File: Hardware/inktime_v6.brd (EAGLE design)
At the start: 46 x 35 mm, 89 parts, among them IC1 BQ25180YBGR, IC2 DRV2605YZFR, IC3 BMA421, IC9 RT6160AWSC, J1 503480-2400, J2 TC2030-IDC, J4 KH-TYPE-C-16P, Q3 DMG2305UX-7, U1 nRF52840-QIAA-R, U3 MAX17048G+T10, X1 32MHz, X2 32.768kHz

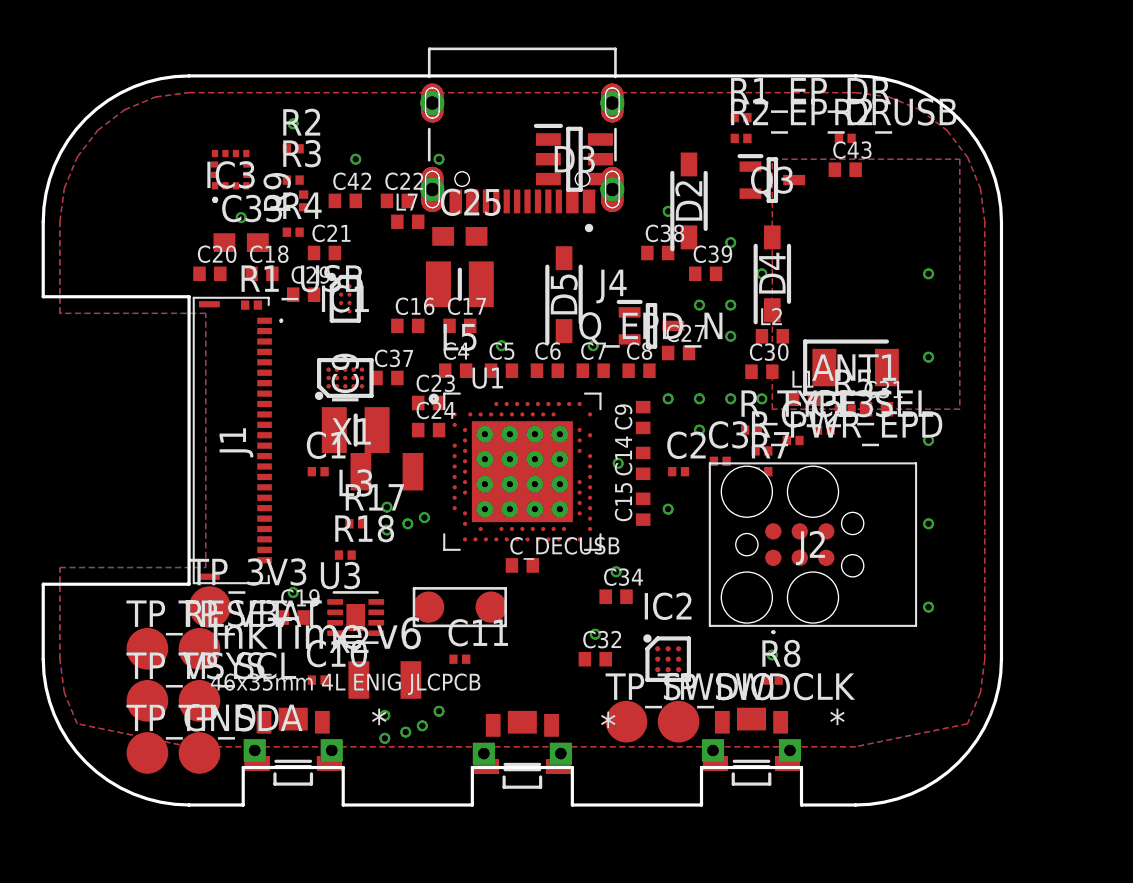
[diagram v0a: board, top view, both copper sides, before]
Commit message: Update BOM and CPL from final PCB
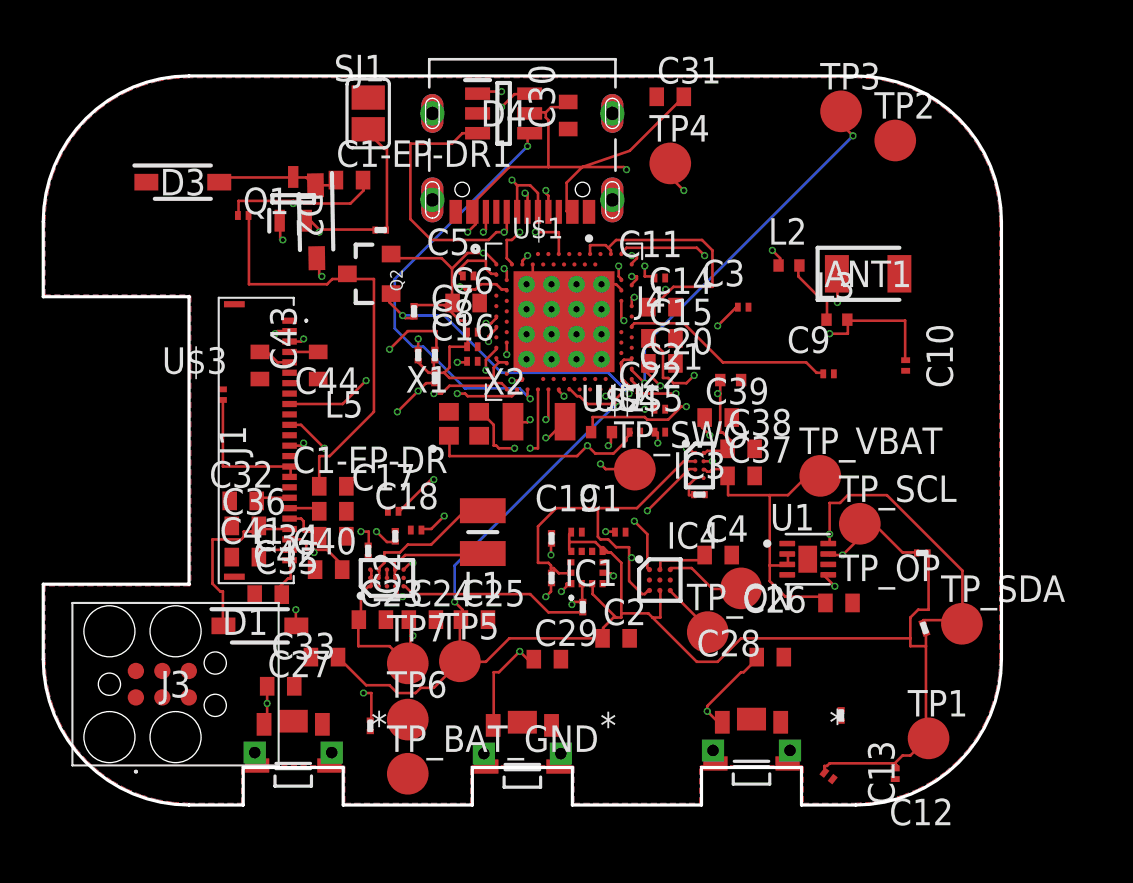
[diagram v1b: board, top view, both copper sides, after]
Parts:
- removed C_DECUSB: 4.7uF, inktime_v5:PERFECT_0402_0402
- removed D5: MBR0530, inktime_v5:ESP32_C6_LIBRARY_5_SOD3716X135N
- removed IC9: RT6160AWSC, inktime_v5:RT6160AWSC_BGA15C40P3X5_140X230X60
- removed J2: TC2030-IDC, inktime_v5:TC2030-IDC_TC2030IDC
- removed L7: 470mOhm, inktime_v5:PERFECT_0402_0402
- removed MOT1: LCM1027B3605F, inktime_v5:WIRE
- removed Q3: DMG2305UX-7, inktime_v5:ESP32_C6_LIBRARY_6_SOT65P210X110-3N
- removed Q_EPD_N: SI1308EDL-T1-GE3, inktime_v5:ESP32_C6_LIBRARY_6_SOT65P210X110-3N
- removed R17, R18: 3.3k, inktime_v5:NORDIC_NRF_2_RESC0201_N
- removed R1_EP_DR, R2_EP_DR, R_PWR_EPD: 10k, inktime_v5:NORDIC_NRF_2_RESC0201_N
- removed R1_USB, R2_USB: 5.1k, inktime_v5:NORDIC_NRF_2_RESC0201_N
- removed R_TYPE_SEL: 2.2, inktime_v5:NORDIC_NRF_2_RESC0201_N
- removed SW_DN, SW_ENT, SW_UP: SW_PUSH, inktime_v5:2025-10-22_07-23-44_LIBRARY_SW_EVP-AKE31A_PAN
- removed TP_3V3, TP_GND, TP_RESET, TP_SWDCLK, TP_SWDIO, TP_VSYS: TP, inktime_v5:HECTOR_WATCH_1_TP20R
- removed U3: MAX17048G+T10, inktime_v5:ESP32_C6_LIBRARY_SON50P200X200X80-9N
- added C1-EP-DR: 10uF, dan-tudose-lib:ESP32_C6_LIBRARY_1_ESP32_WROVER_EAGLE-LTSPICE_C0402
- added C1-EP-DR1: 4.7uF/25V, dan-tudose-lib:ESP32_C6_LIBRARY_1_ESP32_WROVER_EAGLE-LTSPICE_C0402
- added C26: 0.1uF, dan-tudose-lib:ESP32_C6_LIBRARY_1_ESP32_WROVER_EAGLE-LTSPICE_C0402
- added C28: 1uF, dan-tudose-lib:ESP32_C6_LIBRARY_1_ESP32_WROVER_EAGLE-LTSPICE_C0402
- added C35, C36, C40, C41, C44: 1uF/50V, dan-tudose-lib:ESP32_C6_LIBRARY_1_ESP32_WROVER_EAGLE-LTSPICE_C0402
- added D1: ESP32_C6_LIBRARY_5_MBR0530, dan-tudose-lib:ESP32_C6_LIBRARY_5_SOD3716X135N
- added IC4: DRV2605YZFR_DRV2605YZFR, dan-tudose-lib:DRV2605YZFR_BGA9C50P3X3_144X144X62
- added J3: TC2030-IDC_TC2030-IDC, dan-tudose-lib:TC2030-IDC_TC2030IDC
- added Q1: ESP32_C6_LIBRARY_6_SI1308EDL-T1-GE3, dan-tudose-lib:ESP32_C6_LIBRARY_6_SOT65P210X110-3N
- added Q2: 20V/4.2A/52mΩ/1.4W, dan-tudose-lib:ESP32_C6_LIBRARY_4_ESP32_C6_LIBRARY_4_ESP32_C6_LIBRARY_4_ESP32_C6_LIBRARY_4_ESP32_WROVER_SPARKFUN-DISCRE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
- added R1: 0, dan-tudose-lib:CPF0201D7K68C1_0201
- added R10, R11, R12, R13, R14, R16: 10K, dan-tudose-lib:CPF0201D7K68C1_0201
- added R6: 0.47, dan-tudose-lib:CPF0201D7K68C1_0201
- added SJ1: 0, dan-tudose-lib:ESP32_C6_LIBRARY_7_JUMPER_SJ
- added SW1, SW2, SW3: 2025-10-22_07-23-44_LIBRARY_EVP-AKE31ASW_EVP-AKE31A_PAN, dan-tudose-lib:2025-10-22_07-23-44_LIBRARY_SW_EVP-AKE31A_PAN
- added TP1, TP2, TP3, TP4, TP5, TP6, TP7, TP_BAT_GND, TP_ON, TP_OP, TP_SWO: HECTOR_WATCH_1_TPTP20R, dan-tudose-lib:HECTOR_WATCH_1_TP20R
- added U$1: NORDIC_NRF_4_NRF52840_QF, dan-tudose-lib:NORDIC_NRF_4_AQFN50P700X700X85_HS-74N
- added U$2: 3.9nH, dan-tudose-lib:NORDIC_NRF_2_RESC0402_L
- added U$3: 1uF/50V, dan-tudose-lib:NORDIC_NRF_3_RESC0201_L
- added U$4, U$5: 12pF, dan-tudose-lib:NORDIC_NRF_3_RESC0201_L
- ANT1: value 2450AT18B100E -> 2450AT18B100E_2450AT18B100E; device inktime_v5:2450AT18B100E_ANTC3216X140N -> dan-tudose-lib:2450AT18B100E_ANTC3216X140N
- C1: value 12pF -> 1pF; device inktime_v5:NORDIC_NRF_2_RESC0201_N -> dan-tudose-lib:NORDIC_NRF_3_RESC0201_L
- C10: value 12pF -> N.C.; device inktime_v5:NORDIC_NRF_2_RESC0201_N -> dan-tudose-lib:NORDIC_NRF_3_RESC0201_L
- C11: value 12pF -> 100pF; device inktime_v5:NORDIC_NRF_2_RESC0201_N -> dan-tudose-lib:NORDIC_NRF_3_RESC0201_L
- C12: value 820pF -> 100nF; device inktime_v5:NORDIC_NRF_2_RESC0201_N -> dan-tudose-lib:NORDIC_NRF_3_RESC0201_L
- C13: value 1pF -> N.C.; device inktime_v5:NORDIC_NRF_2_RESC0201_N -> dan-tudose-lib:NORDIC_NRF_3_RESC0201_L
- C14, C6: value 100nF -> 4.7µF; device inktime_v5:PERFECT_0402_0402 -> dan-tudose-lib:ESP32_C6_LIBRARY_1_ESP32_WROVER_EAGLE-LTSPICE_C0402
- C15: value 100nF -> 1.0µF; device inktime_v5:PERFECT_0402_0402 -> dan-tudose-lib:ESP32_C6_LIBRARY_1_ESP32_WROVER_EAGLE-LTSPICE_C0402
- C16: value 4.7uF -> 47nF; device inktime_v5:PERFECT_0402_0402 -> dan-tudose-lib:NORDIC_NRF_3_RESC0201_L
- C17: value 4.7uF -> 12pF; device inktime_v5:PERFECT_0402_0402 -> dan-tudose-lib:NORDIC_NRF_3_RESC0201_L
- C18: value 47nF -> 12pF; device inktime_v5:PERFECT_0402_0402 -> dan-tudose-lib:NORDIC_NRF_3_RESC0201_L
- C19, C5: device inktime_v5:PERFECT_0402_0402 -> dan-tudose-lib:NORDIC_NRF_3_RESC0201_L
- C2: value 12pF -> 0.1uF; device inktime_v5:NORDIC_NRF_2_RESC0201_N -> dan-tudose-lib:ESP32_C6_LIBRARY_1_ESP32_WROVER_EAGLE-LTSPICE_C0402
- C20: value 4.7uF -> 4.7µF; device inktime_v5:PERFECT_0402_0402 -> dan-tudose-lib:ESP32_C6_LIBRARY_1_ESP32_WROVER_EAGLE-LTSPICE_C0402
- C21: value 1uF -> 4.7µF; device inktime_v5:PERFECT_0402_0402 -> dan-tudose-lib:NORDIC_NRF_3_RESC0402_L
- C22: value 0.1uF -> N.C.; device inktime_v5:PERFECT_0402_0402 -> dan-tudose-lib:NORDIC_NRF_3_RESC0201_L
- C23, C24, C38: device inktime_v5:PERFECT_0402_0402 -> dan-tudose-lib:ESP32_C6_LIBRARY_1_ESP32_WROVER_EAGLE-LTSPICE_C0402
- C25, C33: device inktime_v5:NORDIC_NRF_2_RESC0603_N -> dan-tudose-lib:ESP32_C6_LIBRARY_1_ESP32_WROVER_EAGLE-LTSPICE_C0402
- C27, C29: value 1uF/50V -> 1uF; device inktime_v5:PERFECT_0402_0402 -> dan-tudose-lib:ESP32_C6_LIBRARY_1_ESP32_WROVER_EAGLE-LTSPICE_C0402
- C3: device inktime_v5:NORDIC_NRF_2_RESC0201_N -> dan-tudose-lib:NORDIC_NRF_3_RESC0201_L
- C30: value 0.1uF/50V -> 4.7uF; device inktime_v5:PERFECT_0402_0402 -> dan-tudose-lib:ESP32_C6_LIBRARY_1_ESP32_WROVER_EAGLE-LTSPICE_C0402
- C31: value 1uF/50V -> 0.1uF; device inktime_v5:PERFECT_0402_0402 -> dan-tudose-lib:ESP32_C6_LIBRARY_1_ESP32_WROVER_EAGLE-LTSPICE_C0402
- C32: value 1uF -> 1uF/50V; device inktime_v5:PERFECT_0402_0402 -> dan-tudose-lib:ESP32_C6_LIBRARY_1_ESP32_WROVER_EAGLE-LTSPICE_C0402
- C34, C43: value 0.1uF -> 1uF/50V; device inktime_v5:PERFECT_0402_0402 -> dan-tudose-lib:ESP32_C6_LIBRARY_1_ESP32_WROVER_EAGLE-LTSPICE_C0402
- C37: value 10uF -> 1uF; device inktime_v5:PERFECT_0402_0402 -> dan-tudose-lib:ESP32_C6_LIBRARY_1_ESP32_WROVER_EAGLE-LTSPICE_C0402
- C39: value 100nF -> 10uF; device inktime_v5:PERFECT_0402_0402 -> dan-tudose-lib:ESP32_C6_LIBRARY_1_ESP32_WROVER_EAGLE-LTSPICE_C0402
- C4: value 100nF -> 1uF; device inktime_v5:PERFECT_0402_0402 -> dan-tudose-lib:ESP32_C6_LIBRARY_1_ESP32_WROVER_EAGLE-LTSPICE_C0402
- C42: value 4.7uF -> 1uF/50V; device inktime_v5:PERFECT_0402_0402 -> dan-tudose-lib:ESP32_C6_LIBRARY_1_ESP32_WROVER_EAGLE-LTSPICE_C0402
- C7: value 100pF -> 100nF; device inktime_v5:PERFECT_0402_0402 -> dan-tudose-lib:NORDIC_NRF_3_RESC0201_L
- C8: value 4.7uF -> 100nF; device inktime_v5:PERFECT_0402_0402 -> dan-tudose-lib:NORDIC_NRF_3_RESC0201_L
- C9: value 1uF -> 820pF; device inktime_v5:PERFECT_0402_0402 -> dan-tudose-lib:NORDIC_NRF_3_RESC0201_L
- D2: value MBR0530 -> ESP32_C6_LIBRARY_5_MBR0530; device inktime_v5:ESP32_C6_LIBRARY_5_SOD3716X135N -> dan-tudose-lib:ESP32_C6_LIBRARY_5_SOD3716X135N
- D3: value USBLC6-2SC6Y -> ESP32_C6_LIBRARY_5_MBR0530; device inktime_v5:ESP32_C6_LIBRARY_3_SOT95P280X145-6N -> dan-tudose-lib:ESP32_C6_LIBRARY_5_SOD3716X135N
- D4: value MBR0530 -> ESP32_C6_LIBRARY_3_USBLC6-2SC6Y; device inktime_v5:ESP32_C6_LIBRARY_5_SOD3716X135N -> dan-tudose-lib:ESP32_C6_LIBRARY_3_SOT95P280X145-6N
- IC1: value BQ25180YBGR -> BMA423_BMA423; device inktime_v5:BQ25180YBGR_BGA8C40P2X4_100X155X50 -> dan-tudose-lib:BMA423_BMA423
- IC2: value DRV2605YZFR -> RT6160AWSC_RT6160AWSC; device inktime_v5:DRV2605YZFR_BGA9C50P3X3_144X144X62 -> dan-tudose-lib:RT6160AWSC_BGA15C40P3X5_140X230X60
- IC3: value BMA421 -> BQ25180YBGR_BQ25180YBGR; device inktime_v5:BMA423_BMA423 -> dan-tudose-lib:BQ25180YBGR_BGA8C40P2X4_100X155X50
- J1: value 503480-2400 -> 503480-2400_503480-2400; device inktime_v5:503480-2400_5034802400 -> dan-tudose-lib:503480-2400_5034802400
- J4: value KH-TYPE-C-16P -> KH-TYPE-C-16P_KH-TYPE-C-16P; device inktime_v5:KH-TYPE-C-16P_KINGHELM_KH-TYPE-C-16P -> dan-tudose-lib:KH-TYPE-C-16P_KINGHELM_KH-TYPE-C-16P
- L1: value 3.9nH -> MLP2016SR47MT0S1_FTC252012SR47MBCA; device inktime_v5:PERFECT_0402_0402 -> dan-tudose-lib:MLP2016SR47MT0S1_INDC2016X100N
- L2: value 15nH -> 10µH; device inktime_v5:PERFECT_0402_0402 -> dan-tudose-lib:NORDIC_NRF_2_RESC0402_L
- L3: value 10uH -> 10µH; device inktime_v5:MLP2016SR47MT0S1_INDC2016X100N -> dan-tudose-lib:NORDIC_NRF_2_RESC0402_L
- L5: device inktime_v5:MLP2016SR47MT0S1_INDC2016X100N -> dan-tudose-lib:NORDIC_NRF_2_RESC0201_L
- R2, R3: device inktime_v5:NORDIC_NRF_2_RESC0201_N -> dan-tudose-lib:CPF0201D7K68C1_0201
- R4: value 0 -> 3K3; device inktime_v5:NORDIC_NRF_2_RESC0201_N -> dan-tudose-lib:CPF0201D7K68C1_0201
- R5: value 10k -> 3K3; device inktime_v5:NORDIC_NRF_2_RESC0201_N -> dan-tudose-lib:CPF0201D7K68C1_0201
- R7: value 10k -> 2.2; device inktime_v5:NORDIC_NRF_2_RESC0201_N -> dan-tudose-lib:CPF0201D7K68C1_0201
- R8, R9: value 10k -> 10K; device inktime_v5:NORDIC_NRF_2_RESC0201_N -> dan-tudose-lib:CPF0201D7K68C1_0201
- TP_SCL, TP_SDA, TP_VBAT: value TP -> HECTOR_WATCH_1_TPTP20R; device inktime_v5:HECTOR_WATCH_1_TP20R -> dan-tudose-lib:HECTOR_WATCH_1_TP20R
- U1: value nRF52840-QIAA-R -> ESP32_C6_LIBRARY_MAX17048G+T10; device inktime_v5:NORDIC_NRF_4_AQFN50P700X700X85_HS-74N -> dan-tudose-lib:ESP32_C6_LIBRARY_SON50P200X200X80-9N
- X1: device inktime_v5:NORDIC_NRF_1_XTAL_3215_N -> dan-tudose-lib:NORDIC_NRF_BT-XTAL_2016_N
- X2: device inktime_v5:NORDIC_NRF_1_XTAL_3215_N -> dan-tudose-lib:NORDIC_NRF_1_XTAL_3215_N
- moved TP_SDA 37.1 mm to (21.1, -8.80)
- moved R4 33.9 mm to (19.2, -5.40), turned to 270 degrees
- moved TP_SCL 32.8 mm to (16.2, -4.00)
- moved C10 32.0 mm to (18.4, 3.60), turned to 270 degrees
- moved TP_VBAT 30.9 mm to (14.3, -1.70)
- moved C43 27.0 mm to (-9.80, 3.60), turned to 90 degrees
- moved IC3 26.6 mm to (8.50, -1.20)
- moved C27 24.9 mm to (-11.6, -11.8)
- moved R2 24.0 mm to (1.40, -6.60)
- moved L3 23.7 mm to (15.1, 5.80)
- moved R9 23.7 mm to (8.50, -2.60), turned to 270 degrees
- moved C20 22.1 mm to (6.70, 3.70)
- moved R3 21.2 mm to (1.40, -4.70)
- moved C29 21.1 mm to (1.20, -10.5)
- moved C11 20.7 mm to (6.60, 7.80)
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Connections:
- removed net BTN_DN: R7.2, SW_DN.1, U1.P$AC9
- removed net BTN_ENT: R8.2, SW_ENT.1, U1.P$AD22
- removed net BTN_UP: R5.2, SW_UP.1, U1.P$AD8
- removed net DCC_LX: U1.P$B3
- removed net DEC1: C4.1, U1.P$C1
- removed net DECUSB: C_DECUSB.1, U1.P$N24
- removed net EPD_C1: C29.1, J1.2
- removed net EPD_C2: C31.1, J1.1
- removed net EPD_MOSI: J1.21, U1.P$B13
- removed net EPD_PWR_EN: Q3.1, R_PWR_EPD.2, U1.P$Y23
- removed net EPD_SCK: J1.20, U1.P$A12
- removed net FUEL_ALRT: U1.P$J24, U3.5
- removed net HAPTIC_OUT_N: IC2.C3, MOT1.-
- removed net HAPTIC_OUT_P: IC2.A3, MOT1.+
- removed net LX_EPD: D2.1, D4.1, L5.1, Q_EPD_N.3
- removed net RF_ANT: ANT1.1, C12.1, C13.1, C3.1, L1.2, L2.1, U1.P$H23
- removed net RF_LX1: IC9.B2, IC9.B3, L1.1, L3.1
- removed net RF_LX2: IC9.D2, IC9.D3, L2.2, L3.2
- removed net USB_CC1: J4.A5, R1_USB.1
- removed net USB_CC2: J4.B5, R2_USB.1
- removed net USB_DM: D3.2, D3.4, J4.A7, J4.B7, U1.P$AD4
- removed net USB_DP: D3.1, D3.6, J4.A6, J4.B6, U1.P$AD6
- removed net VSYS: C17.1, C20.1, C22.1, C23.1, IC1.B2, IC9.A1, IC9.A2, IC9.A3, L7.1, L7.2, TP_VSYS.TP
- removed net XC1_32K: C1.1, U1.P$B24, X1.1
- removed net XC2_32K: C2.1, U1.P$A23, X1.2
- removed net XL1: C10.1, U1.P$D2, X2.1
- removed net XL2: C11.1, U1.P$F2, X2.2
- removed net nRESET: J2.3, TP_RESET.TP, U1.P$AC13
- new net ALERT: U$1.P$J24, U1.5
- new net D+: D4.4, U$1.P$AD6
- new net D-: D4.6, U$1.P$AD4
- new net DEC3: C11.1, U$1.P$D23
- new net DN: D4.1, J4.A7, J4.B7
- new net DP: D4.3, J4.A6, J4.B6
- new net EPD: J1.15, J1.16, U$3.2
- new net GDR: J1.2, Q1.1, R8.2
- new net GND3: IC1.1, R3.2
- new net LX1: IC2.B2, IC2.B3, L1.1
- new net LX2: IC2.D2, IC2.D3, L1.2
- new net MOSI: J1.14, U$1.P$B13
- new net N$1: C5.1, U$1.P$C1
- new net N$10: IC2.D1, R2.2
- new net N$11: C1-EP-DR1.2, D1.2, L5.2
- new net N$12: IC2.E1, R1.2
- new net N$13: C1-EP-DR1.1, D2.1, D3.2, Q1.3
- new net N$14: C9.1, U$1.P$N24
- new net N$16: IC3.D1, R9.2
- new net N$21: U$1.P$B24, U$4.1, X1.1
- new net N$22: R6.1, SJ1.2
- new net N$24: L2.1, U$1.P$B3
- new net N$3: C20.1, U$1.P$AC5
- new net N$30: C4.1, IC4.A2
- new net N$4: ANT1.1, C1.1, C22.1, U$2.2
- new net N$45: J4.A5, R13.2
- new net N$5: C3.1, U$1.P$H23, U$2.1
- new net N$52: J4.B5, R14.1
- new net N$59: C43.2, J1.4
- new net N$6: L2.2, L3.1
- new net N$60: C44.2, J1.5
- new net N$7: U$1.P$A23, U$5.1, X1.3
- new net N$70: C32.2, J1.18
- new net N$71: C34.2, J1.19
- new net N$72: C35.2, J1.20
- new net N$76: C41.2, J1.23
- new net N$78: C42.2, J1.24
- new net OUT+: IC4.A3, TP_OP.TP
- new net OUT-: IC4.C3, TP_ON.TP
- new net P0.00/XL1: C17.2, U$1.P$D2, X2.1
- new net P0.00/XL2: C18.2, U$1.P$F2, X2.2
- new net P0.04: U$1.P$J1
- new net P0.09: U$1.P$L24
- new net P0.13: C27.1, R10.1, SW1.2, U$1.P$AD8
- new net P0.14: C28.1, R11.1, SW2.2, U$1.P$AC9
- new net P0.19: U$1.P$AC15
- new net P0.20: U$1.P$AD16
- new net P0.21: U$1.P$AC17
- new net P0.22: U$1.P$AD18
- new net P0.23: U$1.P$AC19
- new net P0.24: U$1.P$AD20
- new net P0.25: U$1.P$AC21
- new net P0.26: U$1.P$G1
- new net P0.27: U$1.P$H2
- new net P0.28: U$1.P$B11
- new net P0.29: U$1.P$A10
- new net P0.30: U$1.P$B9
- new net P0.31: U$1.P$A8
- new net P1.01: Q2.1, R16.1, U$1.P$W24, U$1.P$Y23
- new net P1.02: C29.1, R12.1, SW3.2
- new net P1.03: U$1.P$V23
- new net P1.04: U$1.P$U24
- new net P1.05: U$1.P$T23
- new net P1.06: U$1.P$R24
- new net P1.07: U$1.P$P23
- new net P1.09: U$1.P$R1
- new net P1.10: U$1.P$A20
- new net P1.11: U$1.P$B19
- new net P1.12: U$1.P$B17
- new net P1.13: U$1.P$A16
- new net P1.14: U$1.P$B15
- new net P1.15: U$1.P$A14
- new net RESET: TP2.TP, U$1.P$AC13
- new net SCK: J1.13, U$1.P$A12
- new net SWO: TP_SWO.TP, U$1.P$AD22
- new net VREG: C23.1, C24.1, C39.1, IC2.A1, IC2.A2, IC2.A3, IC3.B2, TP7.TP
- net 3V3: now also C12.1, C13.1, C2.1, IC1.10, IC1.3, IC1.7, IC2.E3, IC4.C2, Q2.2, R10.2, R11.2, R12.2, R16.2, R4.1, TP1.TP, TP5.TP, U$1.P$A18, U$1.P$A22, U$1.P$AD14, U$1.P$AD23, U$1.P$B1, U$1.P$W1, U$1.P$Y2; no longer C15.1, C24.1, C32.1, C34.1, C5.1, IC2.C2, IC3.3, IC3.7, IC9.E2, IC9.E3, J2.1, Q3.2, R17.1, R18.1, R2.1, R2.2, R7.1, R8.1, R_PWR_EPD.1, TP_3V3.TP, U1.P$A22, U1.P$AD14, U1.P$AD23, U1.P$B1, U1.P$W1, U1.P$Y2
- net DEC4_6: now also C10.1, C15.1, C16.1, L3.2, U$1.P$B5, U$1.P$E24; no longer C9.1, U1.P$B5, U1.P$E24
- net EPD_3V3: now also C1-EP-DR.1, L5.1, Q2.3; no longer C27.1, C30.1, D4.2, D5.1, J1.24, L5.2, Q3.3, R1_EP_DR.1, R2_EP_DR.1, R_TYPE_SEL.1
- net EPD_BUSY: now also J1.9, U$1.P$AD12; no longer U1.P$AD12
- net EPD_CS: now also J1.12, U$1.P$K2; no longer J1.22, U1.P$K2
- net EPD_DC: now also J1.11, U$1.P$AD10; no longer J1.23, U1.P$AD10
- net EPD_RST: now also J1.10, U$1.P$AC11; no longer U1.P$AC11
- net GND: now also C1-EP-DR.2, C17.1, C18.1, C26.2, C28.2, C30.1, C31.1, C32.1, C34.1, C35.1, C36.1, C40.1, C41.1, C43.1, C44.1, D3.1, D4.2, IC1.8, IC1.9, IC2.B1, IC2.C1, IC2.C2, IC2.C3, IC3.D2, IC4.B1, IC4.B3, J1.17, J1.8, R13.1, R14.2, R7.1, R8.1, SJ1.1, SW1.1, SW2.1, SW3.1, TP6.TP, TP_BAT_GND.TP, U$1.P$74, U$1.P$75, U$1.P$76, U$1.P$77, U$1.P$78, U$1.P$79, U$1.P$80, U$1.P$81, U$1.P$82, U$1.P$83, U$1.P$84, U$1.P$85, U$1.P$86, U$1.P$87, U$1.P$88, U$1.P$89, U$1.P$90, U$1.P$B7, U$1.P$F23, U$3.1, U$4.2, U$5.2, U1.1, U1.4, U1.6, U1.9, X1.2, X1.4; no longer ANT1.2, C17.2, C18.2, C30.2, C31.2, C32.2, C34.2, C42.2, C43.2, C_DECUSB.2, D3.3, IC1.D1, IC1.D2, IC2.B3, IC3.1, IC3.8, IC3.9, IC9.B1, IC9.C1, IC9.C2, IC9.C3, J2.5, Q_EPD_N.2, R1_EP_DR.2, R1_USB.2, R2_EP_DR.2, R2_USB.2, R3.2, R9.2, R_TYPE_SEL.2, SW_DN.5, SW_ENT.5, SW_UP.5, TP_GND.TP, U1.P$74, U1.P$75, U1.P$76, U1.P$77, U1.P$78, U1.P$79, U1.P$80, U1.P$81, U1.P$82, U1.P$83, U1.P$84, U1.P$85, U1.P$86, U1.P$87, U1.P$88, U1.P$89, U1.P$90, U1.P$B7, U1.P$F23, U3.1, U3.4, U3.9
- net HAPTIC_EN: now also IC4.A1, U$1.P$U1; no longer IC2.A1, IC2.B1, U1.P$U1
- net IMU_INT1: now also IC1.5, U$1.P$N1; no longer IC3.5, U1.P$N1
- net IMU_INT2: now also IC1.6, U$1.P$P2; no longer IC3.6, U1.P$P2
- net PMIC_INT: now also IC3.A1, U$1.P$T2; no longer IC1.A1, U1.P$T2
- net PREVGH: now also C36.2, D1.1, J1.21; no longer D2.2
- net PREVGL: now also C40.2, D2.2, J1.22; no longer D5.2
- net RESE: now also J1.3, Q1.2, R6.2; no longer Q_EPD_N.1
- net SCL: now also IC1.12, IC3.B1, IC4.C1, R2.1, U$1.P$M2, U1.7; no longer IC1.B1, IC2.C1, IC3.11, IC3.12, IC9.D1, R18.2, R4.1, U1.P$M2, U3.7
- net SDA: now also IC1.2, IC3.C1, IC4.B2, R1.1, R5.2, U$1.P$L1, U1.8; no longer IC1.C1, IC2.B2, IC3.2, IC3.4, IC9.E1, R17.2, U1.P$L1, U3.8
- net SWDCLK: now also TP3.TP, U$1.P$AA24; no longer J2.4, TP_SWDCLK.TP, U1.P$AA24
- net SWDIO: now also TP4.TP, U$1.P$AC24; no longer J2.2, TP_SWDIO.TP, U1.P$AC24
- net VBAT: now also C26.1, IC3.C2, U1.2, U1.3; no longer C18.1, C38.1, IC1.C2, U3.2, U3.3
- net VBUS: now also C30.2, C31.2, C38.1, D4.5, IC3.A2, U$1.P$AD2; no longer C16.1, C42.1, C43.1, D3.5, IC1.A2, U1.P$AD2
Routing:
- net 3V3: track 0.00 -> 132.0 mm, vias 11 -> 5
- net VBUS: track 0.00 -> 56.4 mm, vias 0 -> 4
- net SDA: track 0.00 -> 49.8 mm, vias 0 -> 4
- net DEC4_6: track 0.00 -> 39.5 mm, vias 0 -> 5
- net P0.13: track 0.00 -> 37.6 mm, vias 0 -> 4
- net P0.14: track 0.00 -> 36.3 mm, vias 0 -> 2
- net SCL: track 0.00 -> 35.2 mm, vias 0 -> 2
- net VREG: track 0.00 -> 31.3 mm, vias 0 -> 3
- net N$7: track 0.00 -> 28.6 mm, vias 0 -> 3
- net N$11: track 0.00 -> 28.0 mm, vias 0 -> 2
- net GDR: track 0.00 -> 27.3 mm, vias 0 -> 3
- net N$45: track 0.00 -> 26.9 mm, vias 0 -> 2
- net P0.00/XL2: track 0.00 -> 25.6 mm, vias 0 -> 3
- net N$4: track 0.00 -> 25.5 mm, vias 0 -> 4
- net ALERT: track 0.00 -> 25.1 mm, vias 0 -> 2
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- removed copper zone on layer 15, net 3V3
- removed copper zone on layer 2, net GND
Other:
- board text removed: "46x35mm 4L ENIG JLCPCB"
- board text removed: "InkTime v6"
